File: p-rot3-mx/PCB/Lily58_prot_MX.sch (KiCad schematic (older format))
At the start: 84 parts, among them J1 LED, J2 4PIN, J3 OLED, P1 i2c_pin, P2 i2c_pin, SW1 SW_PUSH, SW10 SW_PUSH, SW11 SW_PUSH, SW12 SW_PUSH, SW13 SW_PUSH, SW14 SW_PUSH, SW15 SW_PUSH, SW16 SW_PUSH, SW17 SW_PUSH, SW18 SW_PUSH, SW19 SW_PUSH, SW2 SW_PUSH, SW20 SW_PUSH, SW21 SW_PUSH, SW22 SW_PUSH, SW23 SW_PUSH, SW24 SW_PUSH, SW25 SW_PUSH, SW26 SW_PUSH, SW27 SW_PUSH, SW28 SW_PUSH, SW29 SW_PUSH, SW3 SW_PUSH, SW30 ROT_ENC_SW, SW4 SW_PUSH, SW5 SW_PUSH, SW6 SW_PUSH, SW7 SW_PUSH, SW8 SW_PUSH, SW9 SW_PUSH, U1 ProMicro

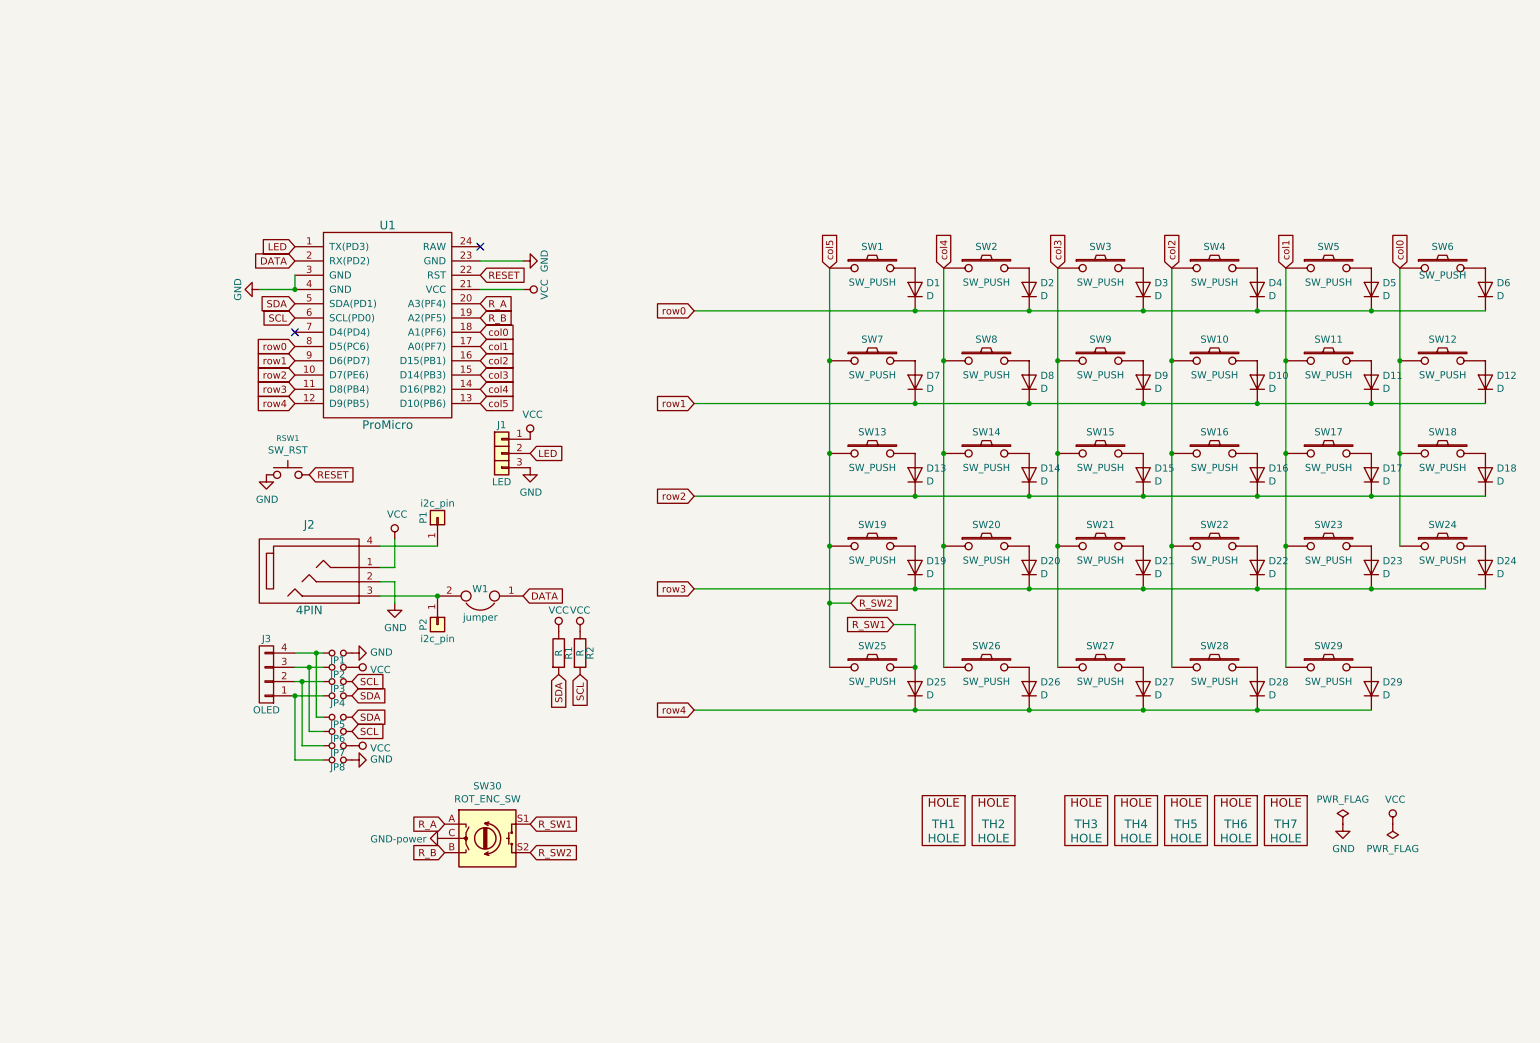
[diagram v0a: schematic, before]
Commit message: added extra encoders to schematic and PCB -- still need to be routed; diodes now SOD
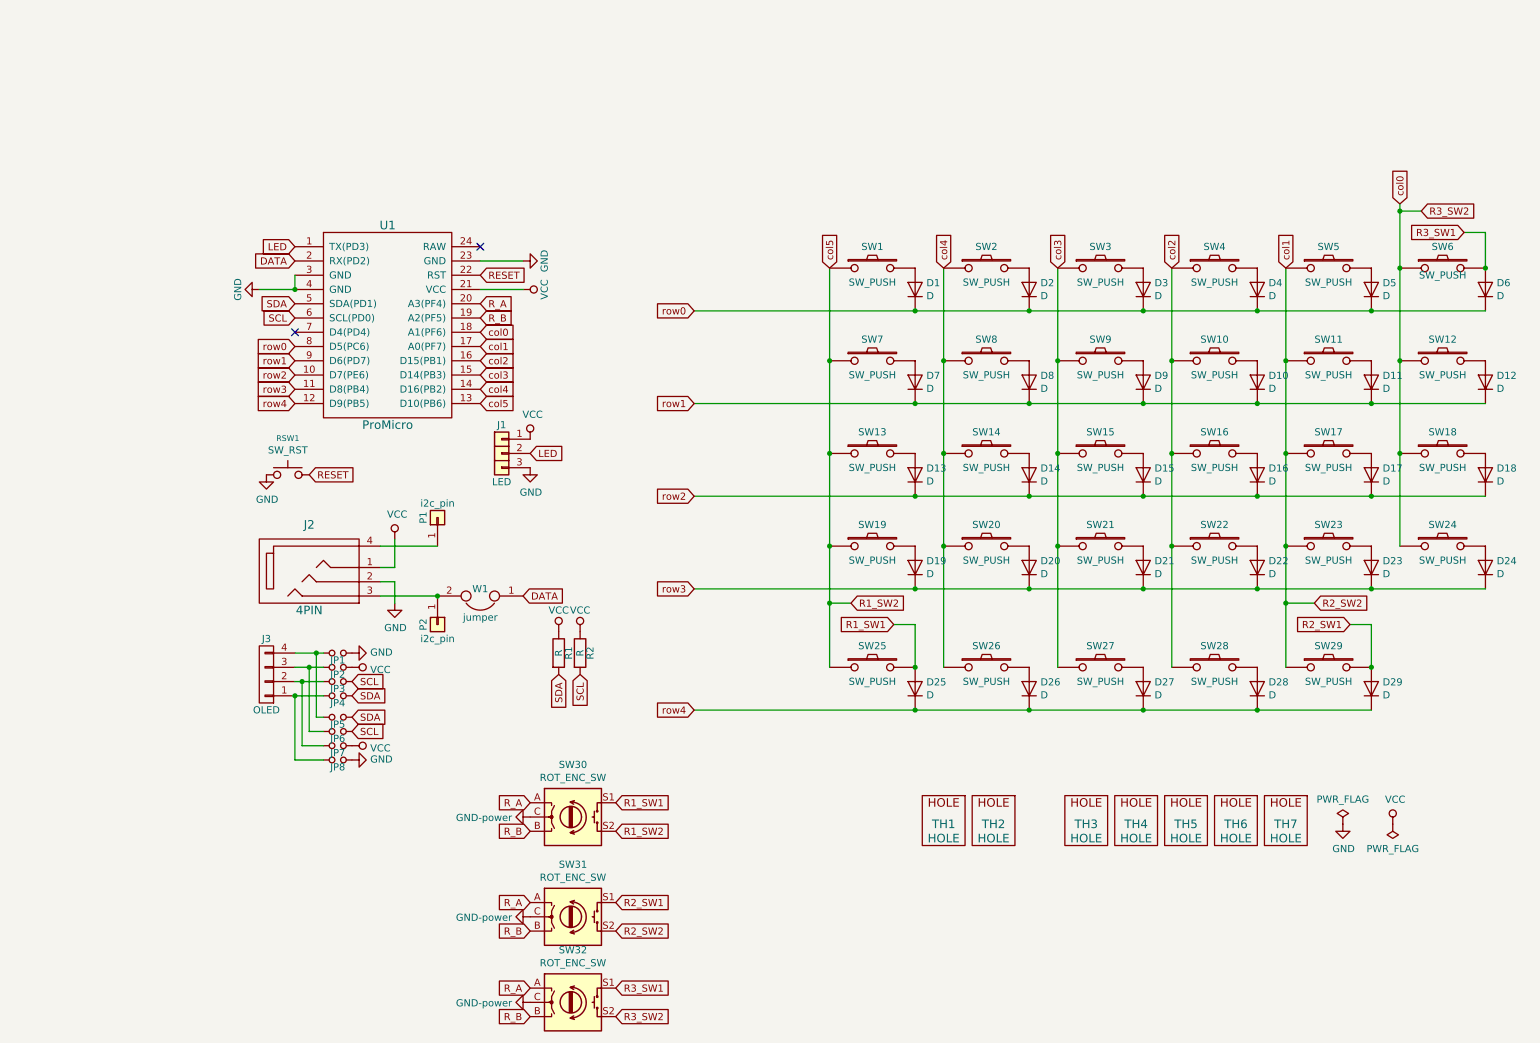
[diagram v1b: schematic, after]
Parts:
- added SW31, SW32: ROT_ENC_SW, Lily58_prot_MX-footprint:RotaryEncoder_Alps_EC11E-Switch_Vertical_H20mm-keebio_modified-no_MP, symbol Lily58_prot_MX-rescue:Device_Rotary_Encoder_Switch
- D1, D10, D11, D12, D13, D14, D15, D16, D17, D18, D19, D2, D20, D21, D22, D23, D24, D25, D26, D27, D28, D29, D3, D4, D5, D6, D7, D8, D9: footprint Lily58_prot_MX-footprint:Diode_TH_SOD123 -> Lily58_prot_MX-footprint:Diode_SOD123
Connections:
- net GND: now also SW31.C, SW32.C
- net R_A: now also SW31.A, SW32.A
- net R_B: now also SW31.B, SW32.B
- net R3_SW1: now reaches D6.2 (A), SW6.2
- net R3_SW1: now also SW32.S1
- net R2_SW1: now reaches D29.2 (A), SW29.2
- net R2_SW1: now also SW31.S1
- net R_SW1 renamed R1_SW1
- net R_SW2 renamed R1_SW2
- net col0 renamed R3_SW2
- net R3_SW2: now also SW32.S2
- net col1 renamed R2_SW2
- net R2_SW2: now also SW31.S2
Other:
- moved on the sheet: SW30

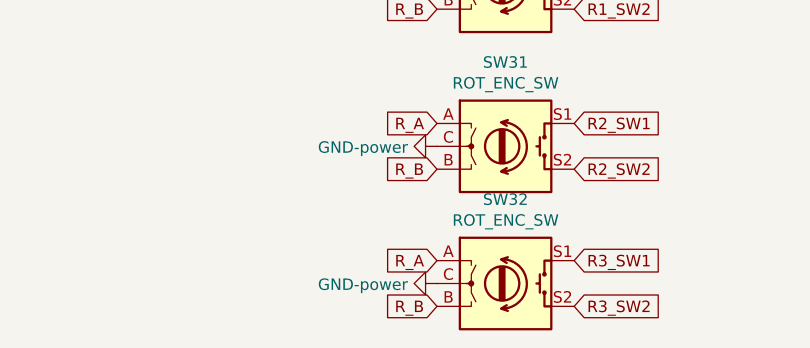
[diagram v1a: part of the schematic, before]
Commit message: added routing for GND to all encoders
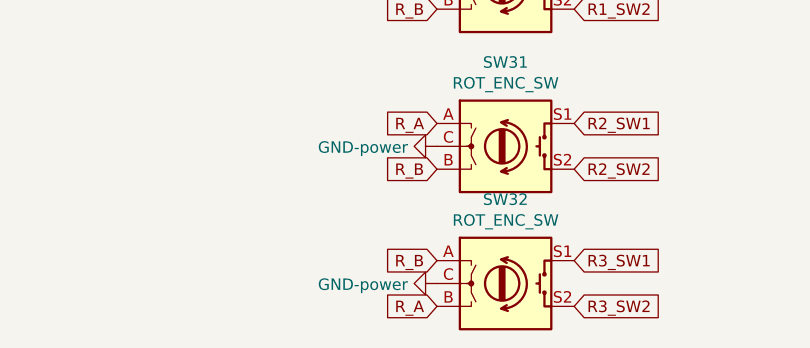
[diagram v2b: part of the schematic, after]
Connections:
- net R_A: now also SW32.B; no longer SW32.A
- net R_B: now also SW32.A; no longer SW32.B
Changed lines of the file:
@@
-	1    0    0    -1
-$EndComp
-$Comp
-L Lily58_prot_MX-rescue:Device_Rotary_Encoder_Switch SW32
-U 1 1 5FED90A3
-P 4500 7400
-F 0 "SW32" H 4500 7767 50  0000 C CNN
-F 1 "ROT_ENC_SW" H 4500 7676 50  0000 C CNN
-F 2 "Lily58_prot_MX-footprint:RotaryEncoder_Alps_EC11E-Switch_Vertical_H20mm-keebio_modified-no_MP" H 4350 7560 50  0001 C CNN
-F 3 "" H 4500 7660 50  0001 C CNN
-	1    4500 7400
 	1    0    0    -1
 $EndComp
@@
 Text GLabel 4200 6900 0    50   Input ~ 0
 R_B
+Text GLabel 4200 7500 0    50   Input ~ 0
+R_A
 Text GLabel 4200 7300 0    50   Input ~ 0
-R_A
-Text GLabel 4200 7500 0    50   Input ~ 0
 R_B
 Text GLabel 4800 6700 2    50   Input ~ 0
@@
 Text GLabel 10750 2000 0    50   Input ~ 0
 R3_SW1
+$Comp
+L Lily58_prot_MX-rescue:Device_Rotary_Encoder_Switch SW32
+U 1 1 5FED90A3
+P 4500 7400
+F 0 "SW32" H 4500 7767 50  0000 C CNN
+F 1 "ROT_ENC_SW" H 4500 7676 50  0000 C CNN
+F 2 "Lily58_prot_MX-footprint:RotaryEncoder_Alps_EC11E-Switch_Vertical_H20mm-keebio_modified-no_MP" H 4350 7560 50  0001 C CNN
+F 3 "" H 4500 7660 50  0001 C CNN
+	1    4500 7400
+	1    0    0    -1
+$EndComp
 $EndSCHEMATC

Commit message: rerouted all switch, encoder, and ground traces
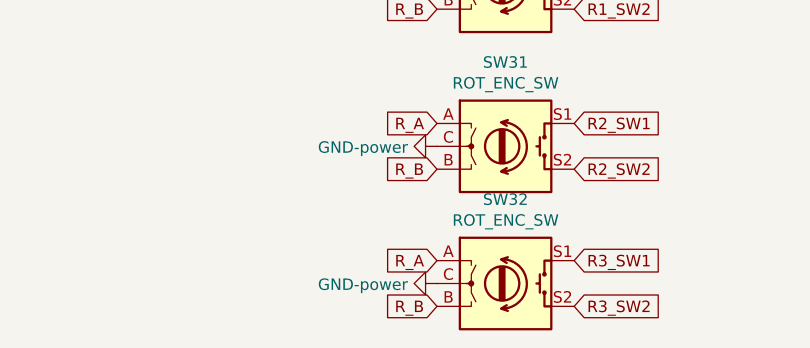
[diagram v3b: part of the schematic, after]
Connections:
- net R_A: now also SW32.A; no longer SW32.B
- net R_B: now also SW32.B; no longer SW32.A
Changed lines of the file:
@@
 Text GLabel 4200 6900 0    50   Input ~ 0
 R_B
+Text GLabel 4200 7300 0    50   Input ~ 0
+R_A
 Text GLabel 4200 7500 0    50   Input ~ 0
-R_A
-Text GLabel 4200 7300 0    50   Input ~ 0
 R_B
 Text GLabel 4800 6700 2    50   Input ~ 0

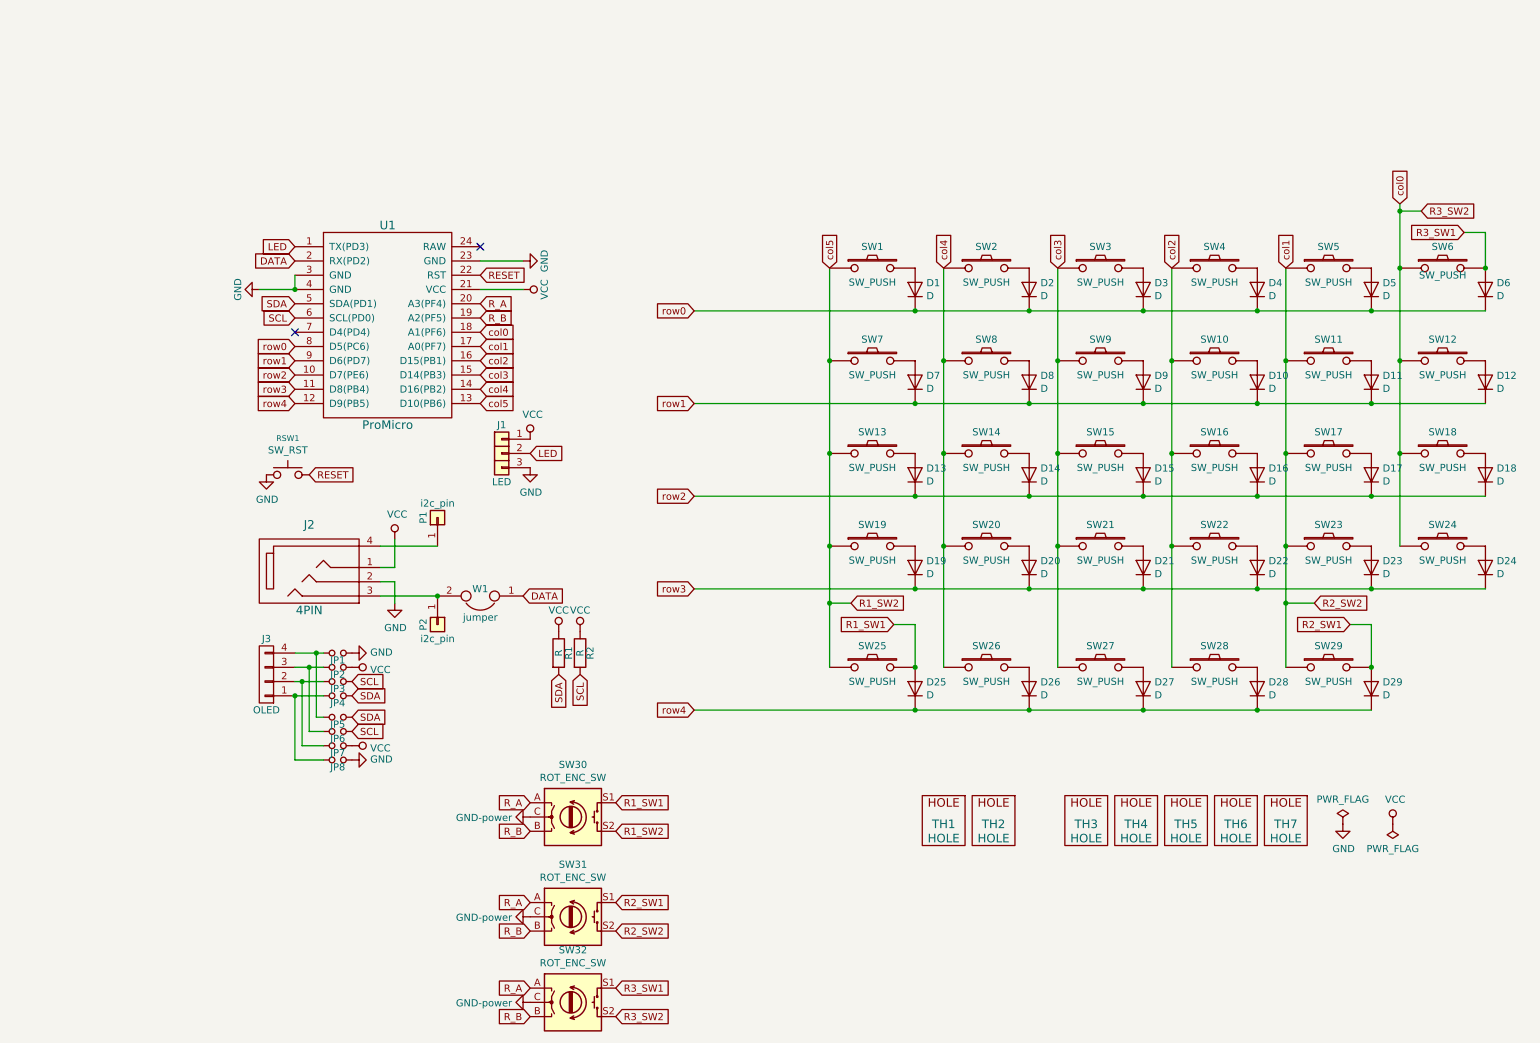
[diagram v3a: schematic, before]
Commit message: added Lily58Glow led footprint to folder
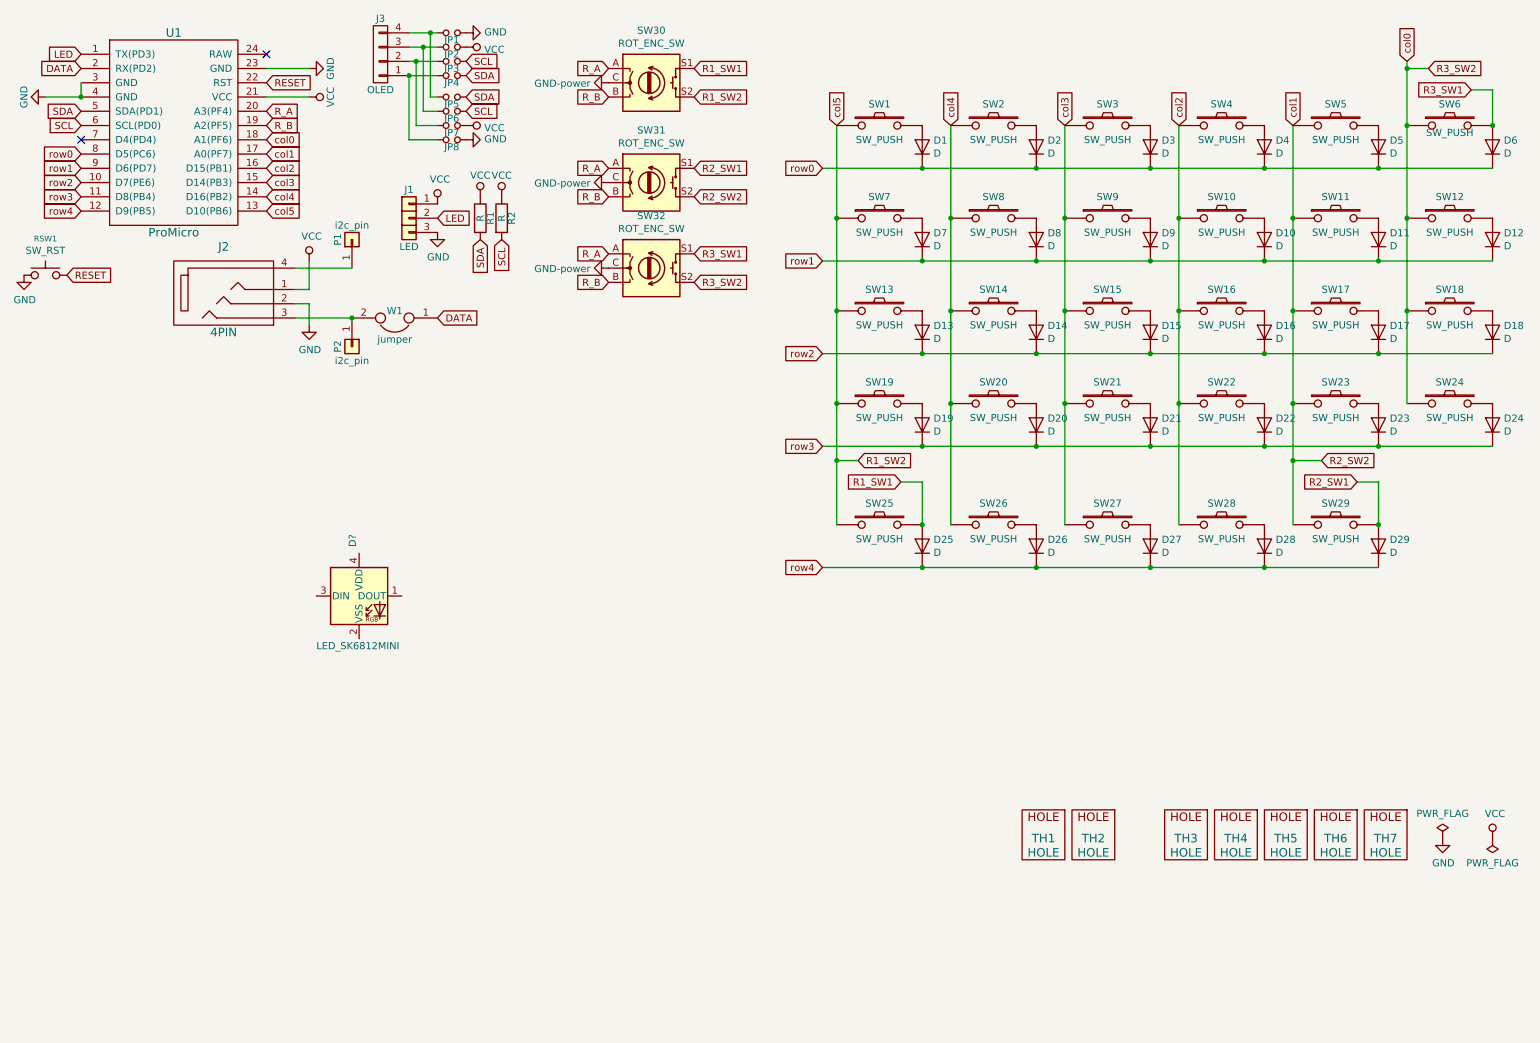
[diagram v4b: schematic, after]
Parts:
- added D?: LED_SK6812MINI, LED_SMD:LED_SK6812MINI_PLCC4_3.5x3.5mm_P1.75mm, symbol Lily58_prot_MX-rescue:LED_SK6812MINI
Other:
- moved on the sheet: D1, D10, D11, D12, D13, D14, D15, D16, D17, D18, D19, D2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
